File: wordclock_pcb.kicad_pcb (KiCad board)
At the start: 2 copper layers, 105.4 x 90.9 mm, 37 parts, among them IC1 ATmega328P, J1 MYUSBCONN5, J2 Stecker 1, J3 Stecker 2, J4 Stecker 3, Q1 2N3904, Q2 2N3904, SW1 MYSWITCH2, SW2 MYSWITCH_reduced, SW3 MYSWITCH_reduced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

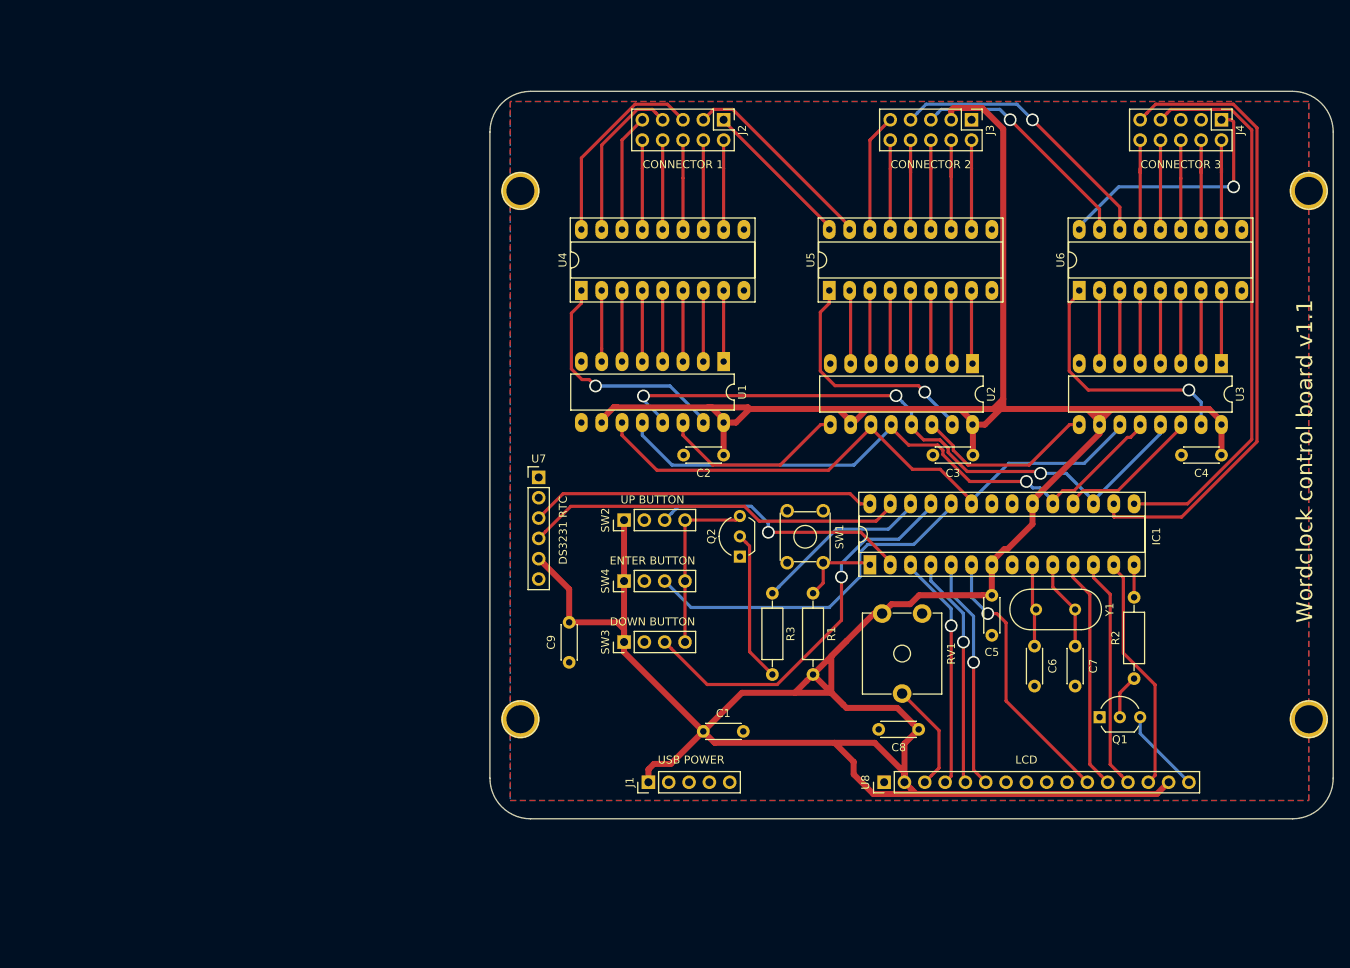
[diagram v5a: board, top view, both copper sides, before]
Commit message: Widen traces and add logos
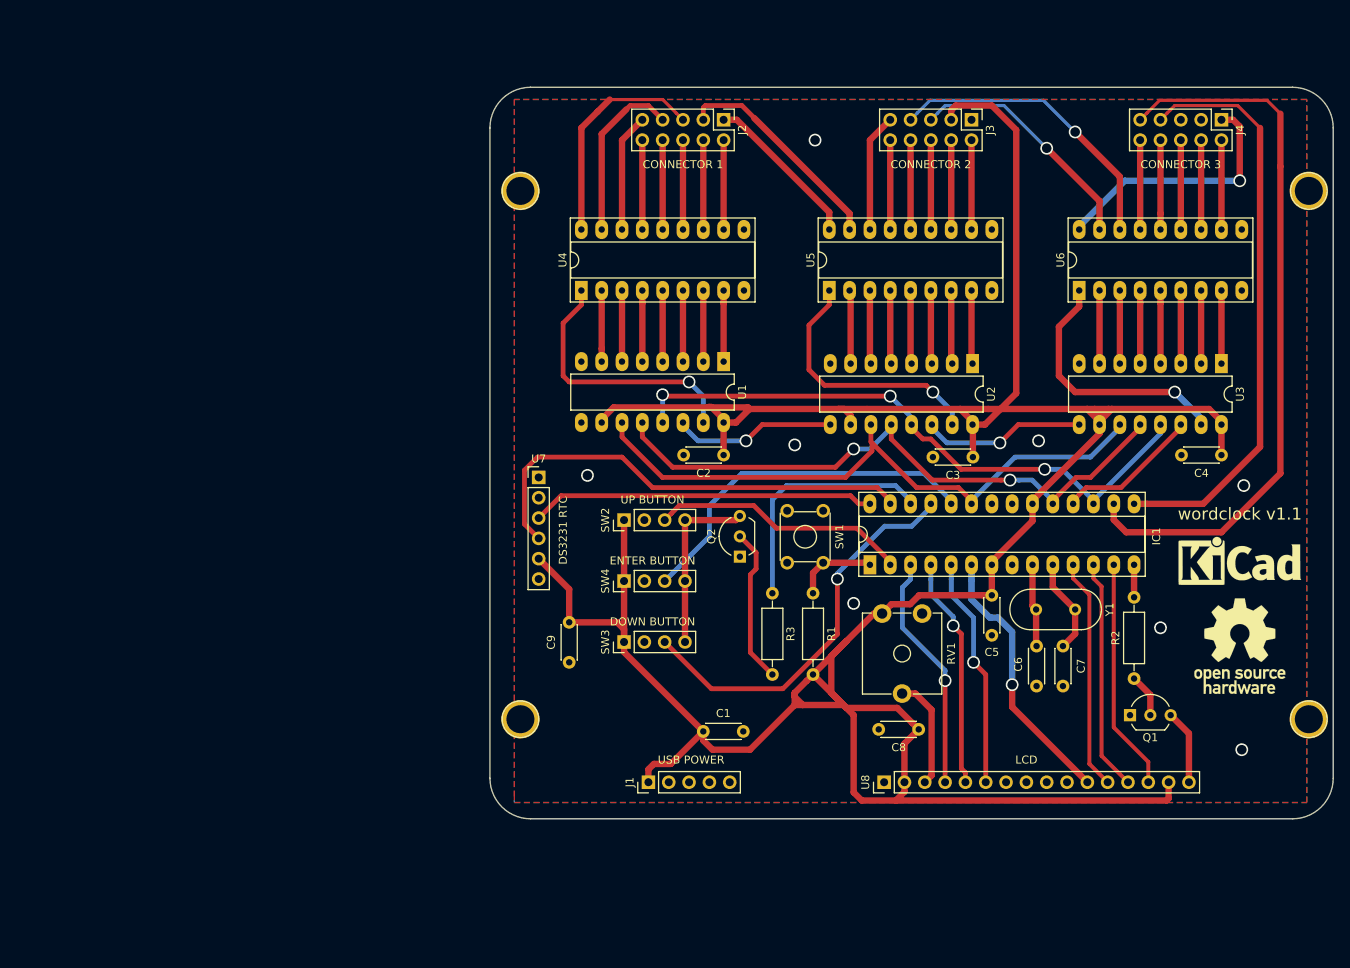
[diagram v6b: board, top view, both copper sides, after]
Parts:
- added REF***: KiCad-Logo_6mm_SilkScreen, Symbols:KiCad-Logo_6mm_SilkScreen, F.Cu at (183.4, 101.6)
- added REF***: OSHW-Logo_11.4x12mm_SilkScreen, Symbols:OSHW-Logo_11.4x12mm_SilkScreen, F.Cu at (183.4, 112.3)
- moved Q1 3.82 mm to (169.7, 120.9)
- moved C7 1.52 mm to (161.3, 112.3)
- moved C3 0.25 mm to (150.0, 88.6)
- moved C6 0.25 mm to (158.0, 112.3)
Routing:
- net AVCC: track 411.2 -> 395.3 mm
- net RGB_HAPPY: track 79.3 -> 90.7 mm
- net SDA: track 47.5 -> 58.3 mm
- net SWITCH_LEDS: track 22.1 -> 30.9 mm
- net OE: track 80.9 -> 77.0 mm
- net Net-(U1-Pad15): track 29.8 -> 33.5 mm
- net RGB_BIRTH: track 69.7 -> 73.1 mm
- net Net-(U1-Pad14): track 23.6 -> 20.4 mm, vias 0 -> 1
- net ZWEI: track 20.6 -> 23.6 mm
- net Net-(U2-Pad15): track 30.2 -> 33.1 mm
- net ZWOELF: track 25.2 -> 27.9 mm
- net ZEHN2: track 35.1 -> 37.7 mm
- net Net-(U2-Pad14): track 22.9 -> 20.5 mm, vias 0 -> 1
- net UHR: track 25.3 -> 27.5 mm
- net SHCP: track 77.0 -> 78.8 mm
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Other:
- board size 105.4 x 90.9 mm -> 105.4 x 91.4 mm
- net class Power: trace_width 0.75 -> 0.8
- board text added: "wordclock v1.1"
- board text removed: "Wordclock control board v1.1"

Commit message: Enlarge text on silkscreen, fix positioning, addpolarity symbols for buttons
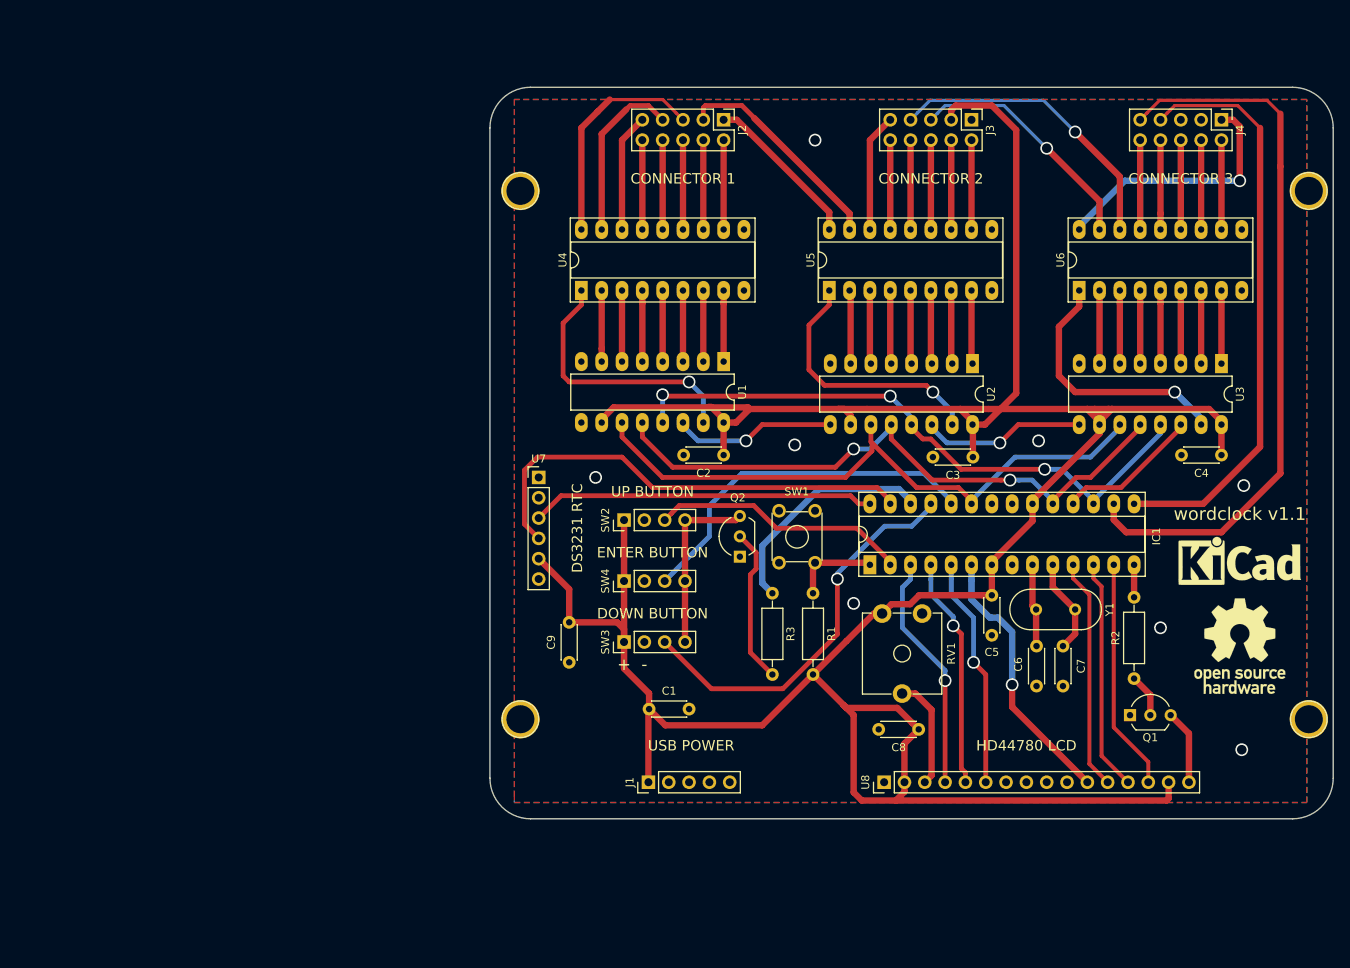
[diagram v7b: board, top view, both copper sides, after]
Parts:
- moved C1 7.33 mm to (109.6, 120.1)
- moved SW1 1.02 mm to (130.3, 95.4)
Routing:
- net AVCC: track 395.3 -> 374.9 mm
- net SWITCH_LEDS: track 30.9 -> 28.9 mm
- net Net-(IC1-Pad1): track 10.3 -> 10.9 mm
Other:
- board text added: "+"
- board text added: "-"
- board text added: "HD44780 LCD"
- board text removed: "LCD"
